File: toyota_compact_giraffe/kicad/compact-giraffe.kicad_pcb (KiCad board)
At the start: 2 copper layers, 42.5 x 24.1 mm, 7 parts, among them J2 MOBILEEYE, J3 MOBILEEYE, P1 panda, U1 Power, U2 USB

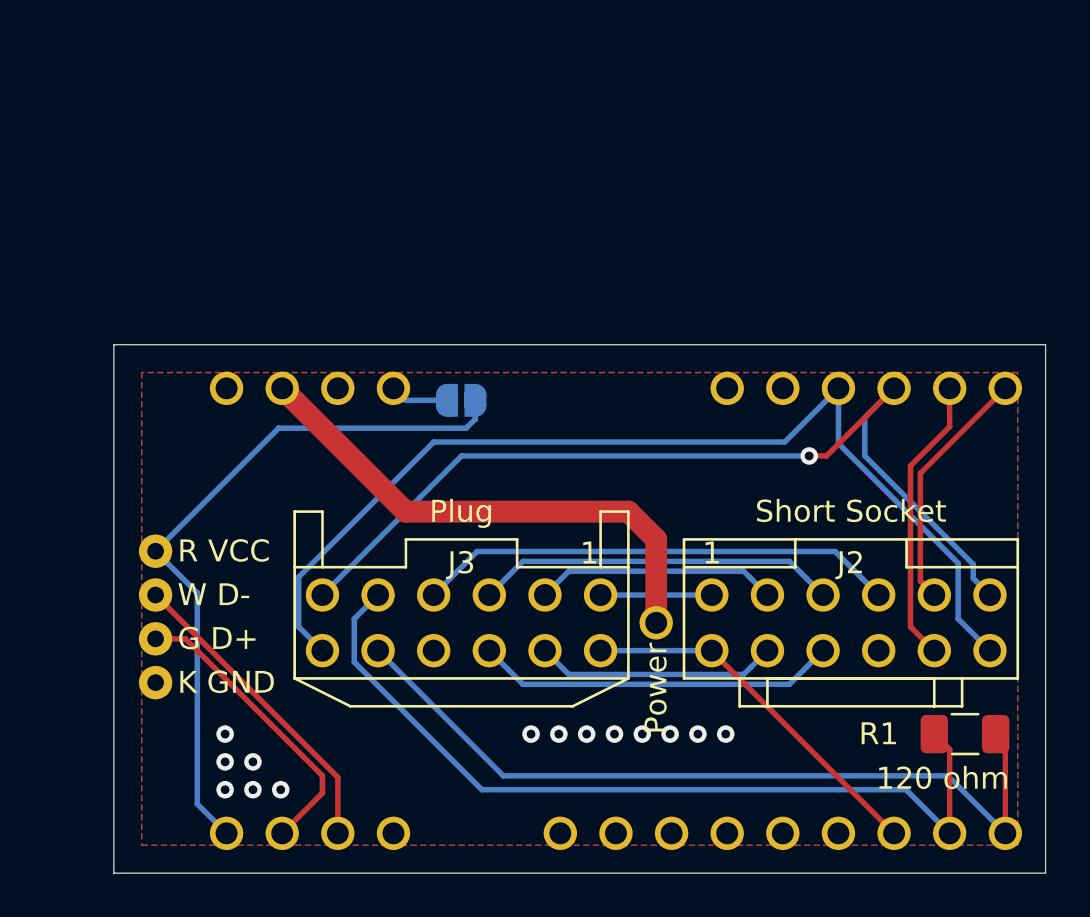
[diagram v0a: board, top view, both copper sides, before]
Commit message: changed texts on board, regenerate gerber
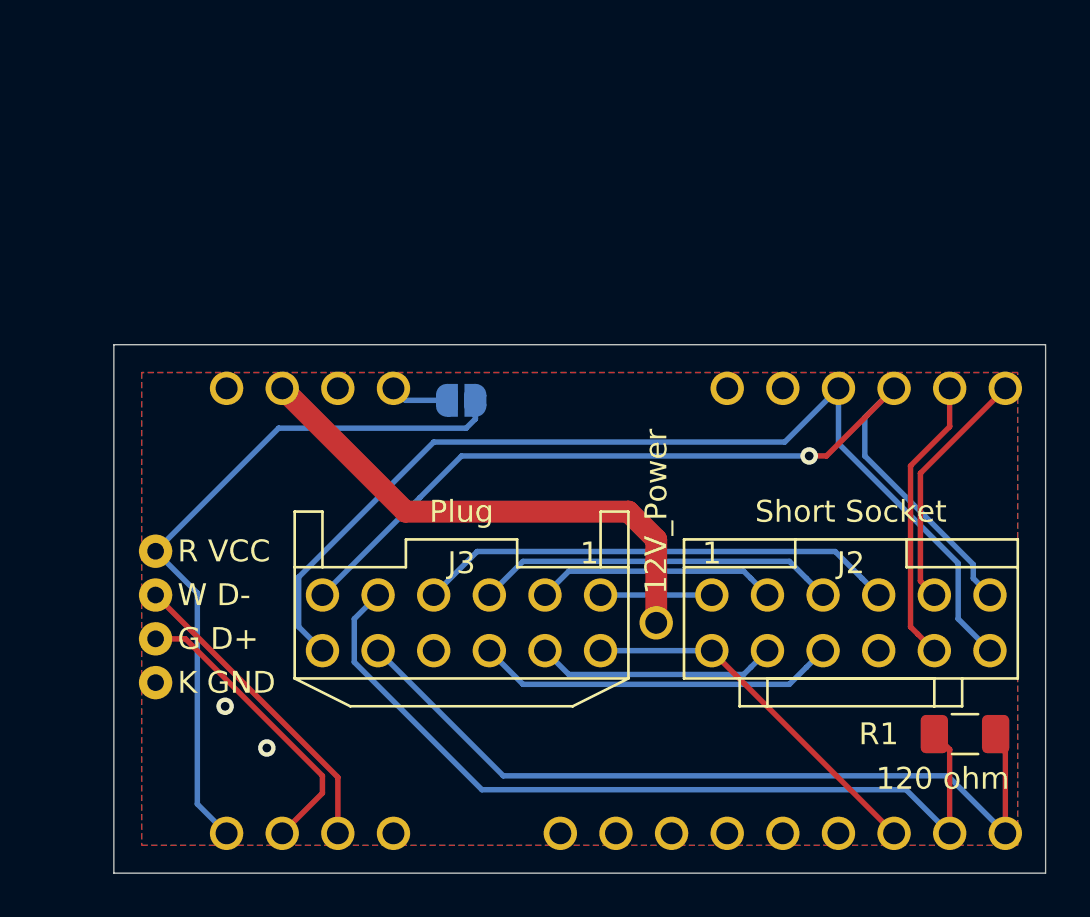
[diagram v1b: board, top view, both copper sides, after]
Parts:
- JP1: value Paw_Boot -> Paw_DFU_Boot
- U1: value Power -> 12V_Power
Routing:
- net /GND: vias 14 -> 2

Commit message: flip back side to front, regen gerber
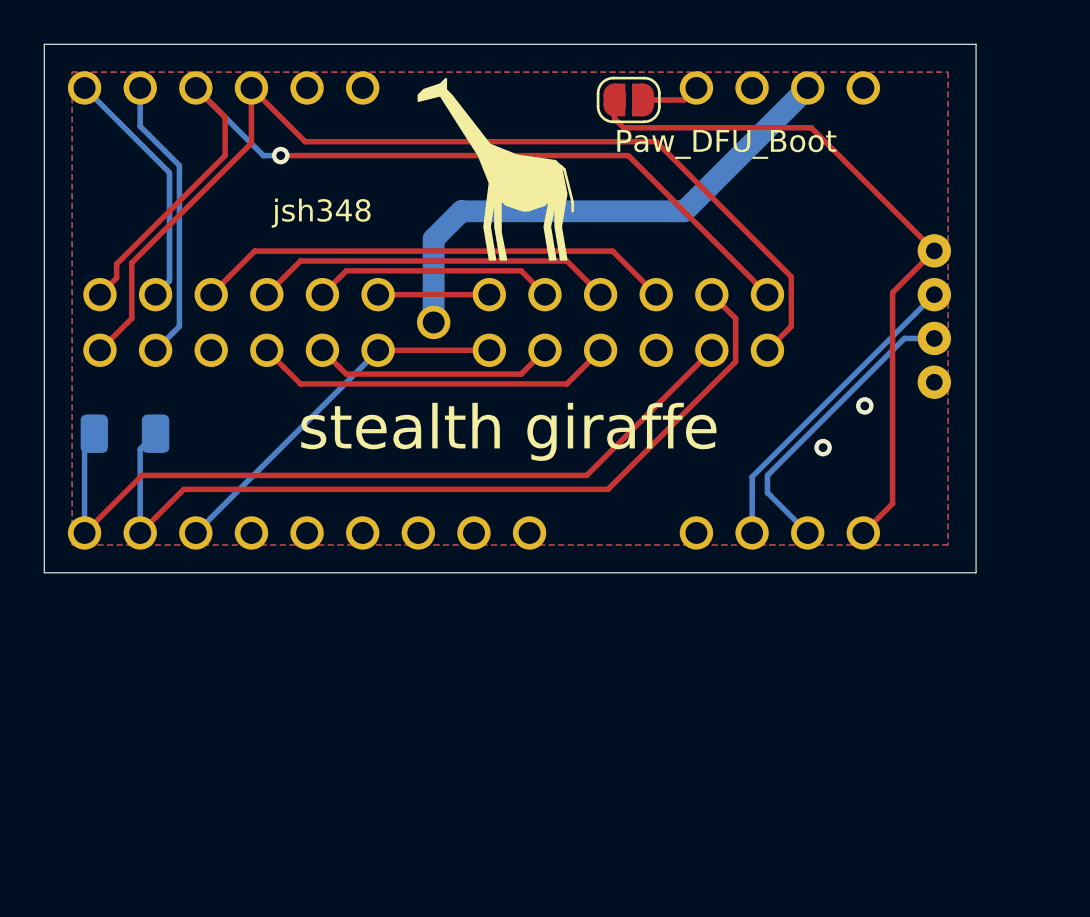
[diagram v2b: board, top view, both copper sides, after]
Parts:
- J2, J3, P1, R1, U1, U2: moved to B.Cu
- JP1: moved to F.Cu
- moved R1 40.7 mm to (101.5, 81.5), turned to 0 degrees
- moved U2 38.1 mm to (138.4, 76.2)
- moved P1 32.1 mm to (135.2, 86.1), turned to 180 degrees
- moved J2 31.1 mm to (106.7, 77.7), turned to 180 degrees
- moved J3 22.5 mm to (129.5, 75.2), turned to 0 degrees
- moved U1 17.1 mm to (115.6, 76.5)
- moved JP1 15.7 mm to (124.5, 66.3), turned to 0 degrees
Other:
- board text added: "stealth giraffe"

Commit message: modifications for v3. trace width, re-routs for easier 12v soldering
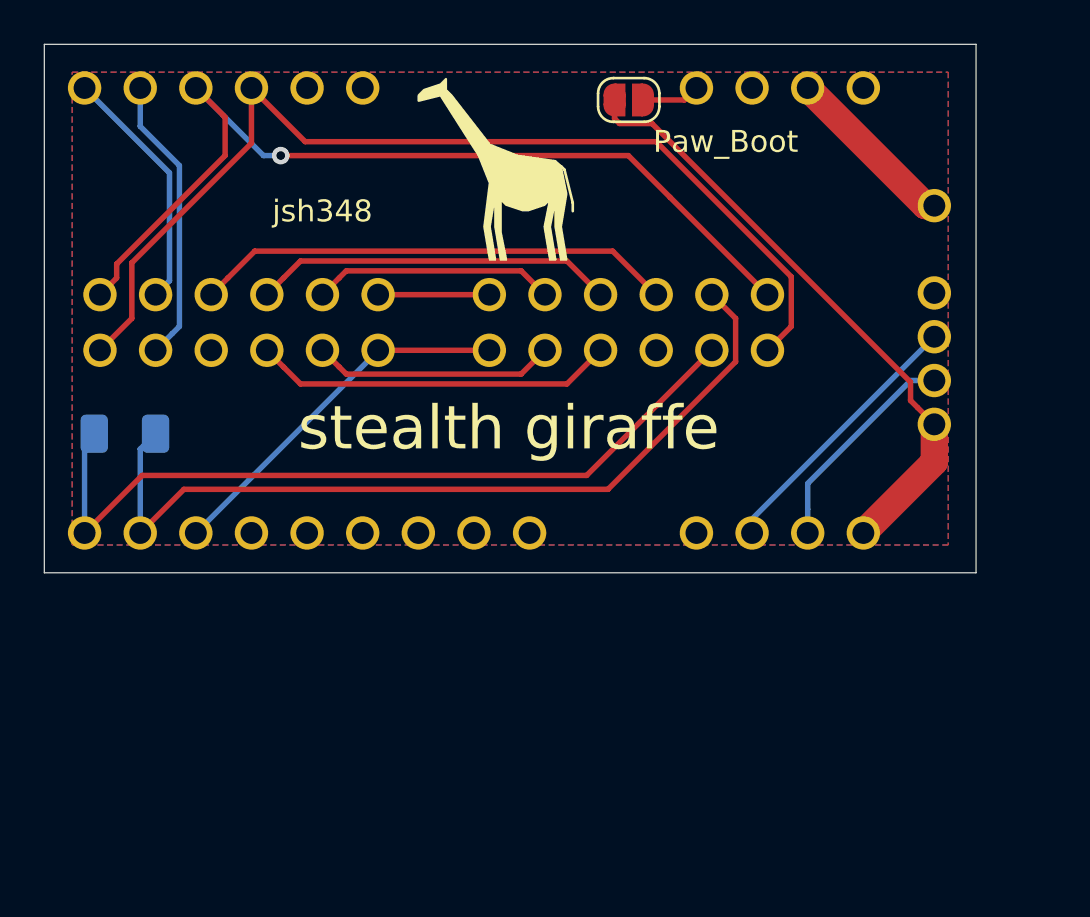
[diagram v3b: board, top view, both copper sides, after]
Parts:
- JP1: value Paw_DFU_Boot -> Paw_Boot
- U1: value 12V_Power -> Power
- moved U1 23.5 mm to (138.4, 71.1), turned to 0 degrees
- moved U2 1.92 mm to (138.4, 78.1), turned to 90 degrees
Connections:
- net Net-(JP1-Pad1) renamed /5V
- P1 pad 10: Net-(P1-Pad10) -> (no net)
- P1 pad 16: Net-(P1-Pad16) -> (no net)
- P1 pad 18: Net-(P1-Pad18) -> (no net)
- P1 pad 19: Net-(P1-Pad19) -> (no net)
- P1 pad 2: Net-(P1-Pad2) -> /D-
- P1 pad 3: Net-(P1-Pad3) -> /D+
- P1 pad 5: Net-(P1-Pad5) -> (no net)
- P1 pad 6: Net-(P1-Pad6) -> (no net)
- P1 pad 7: Net-(P1-Pad7) -> (no net)
- P1 pad 9: Net-(P1-Pad9) -> (no net)
- U2 pad 2: Net-(P1-Pad3) -> /D-
- U2 pad 3: Net-(P1-Pad2) -> /D+
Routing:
- net /12VIN: track 23.7 -> 8.01 mm
- net Net-(P1-Pad3): track 14.3 -> 0.00 mm
- net Net-(P1-Pad2): track 13.6 -> 0.00 mm
- net /D+: track 0.00 -> 12.4 mm
- net /D-: track 0.00 -> 9.99 mm
- net /5V: track 32.2 -> 28.0 mm
- net /GND: vias 2 -> 0
